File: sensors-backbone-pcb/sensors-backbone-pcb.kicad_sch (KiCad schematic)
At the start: 22 parts, among them J1 Conn_01x08, J2 Conn_01x08, J3 Conn_01x08, U1 picoscope-2000, U2 74HC4051, U3 74HC4051, U4 74HC4051, U5 4094

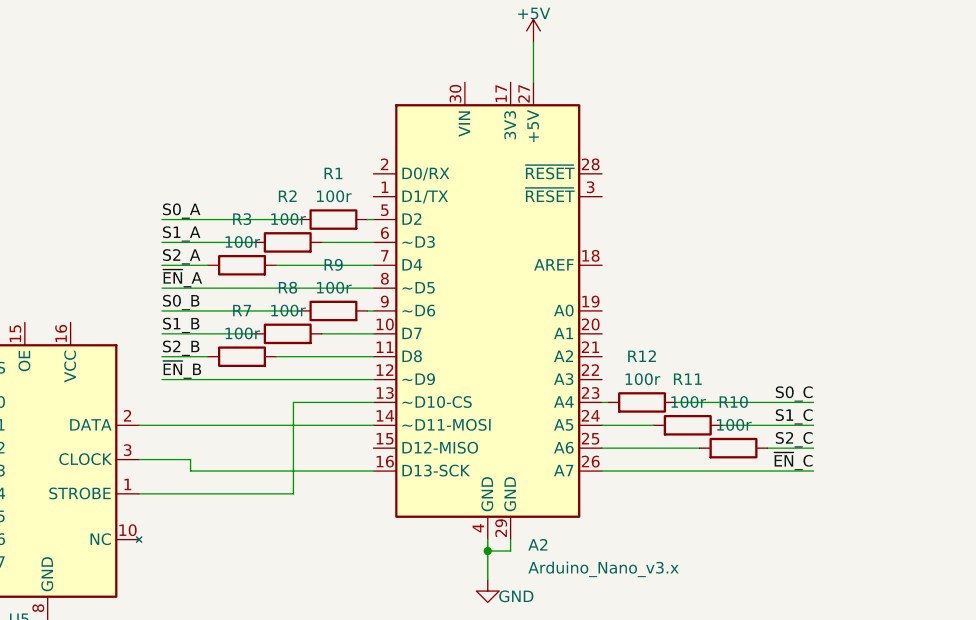
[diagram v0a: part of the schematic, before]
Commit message: Added README for power distribution design
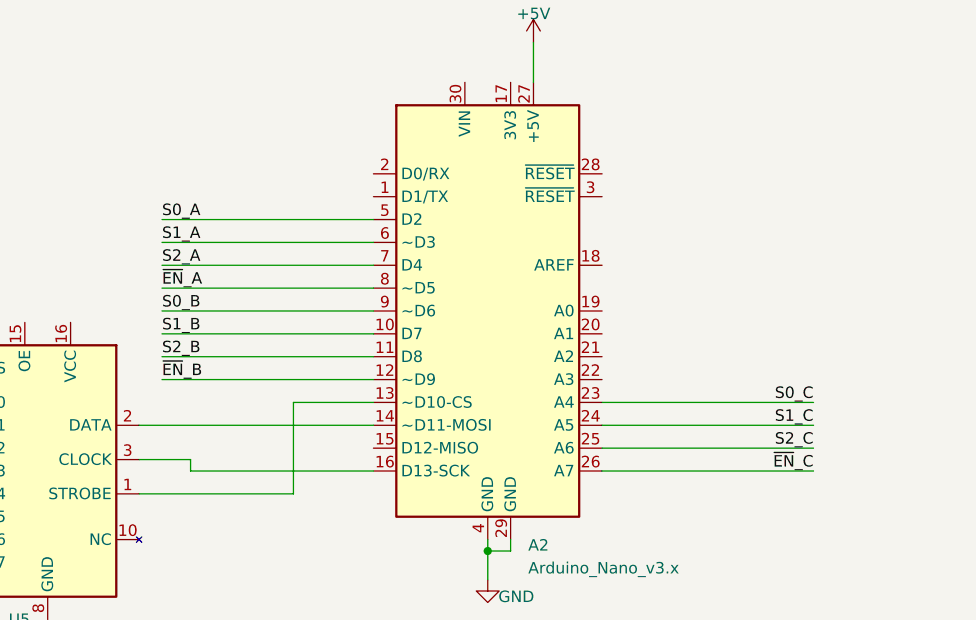
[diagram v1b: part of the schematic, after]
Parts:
- removed R1, R10, R11, R12, R2, R3, R7, R8, R9: 100r, Resistor_SMD:R_0805_2012Metric_Pad1.20x1.40mm_HandSolder, symbol 000_Resistors_Immo:100r
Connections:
- net S0_A: now also A2.5 (D2)
- net S0_B: now also A2.9 (~D6)
- net S0_C: now also A2.23 (A4)
- net S1_A: now also A2.6 (~D3)
- net S1_B: now also A2.10 (D7)
- net S1_C: now also A2.24 (A5)
- net S2_A: now also A2.7 (D4)
- net S2_B: now also A2.11 (D8)
- net S2_C: now also A2.25 (A6)
